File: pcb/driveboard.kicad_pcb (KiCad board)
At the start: 2 copper layers, 147.3 x 94 mm, 53 parts, among them IC1 7411, IC2 7410, P1 AC IN, P2 AC out, P3 5V in, P6 AQV2526, x1 RJ45, x2 RJ45, y1 RJ45, y2 RJ45

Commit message: Use Protel filename extensions for the sake of dirtypcbs.com.
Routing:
- net Net-(R12-Pad2): track 20.9 -> 31.7 mm
- net Net-(Arduino2-Pad2): track 46.4 -> 35.6 mm

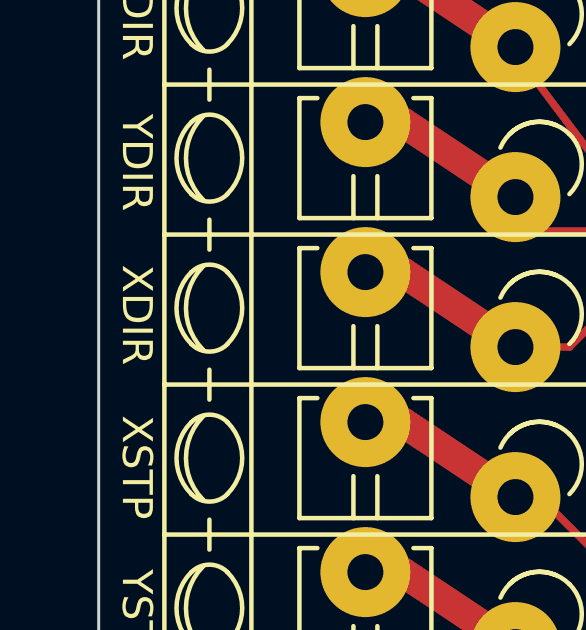
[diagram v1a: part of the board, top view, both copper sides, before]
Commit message: Fix wrong label.
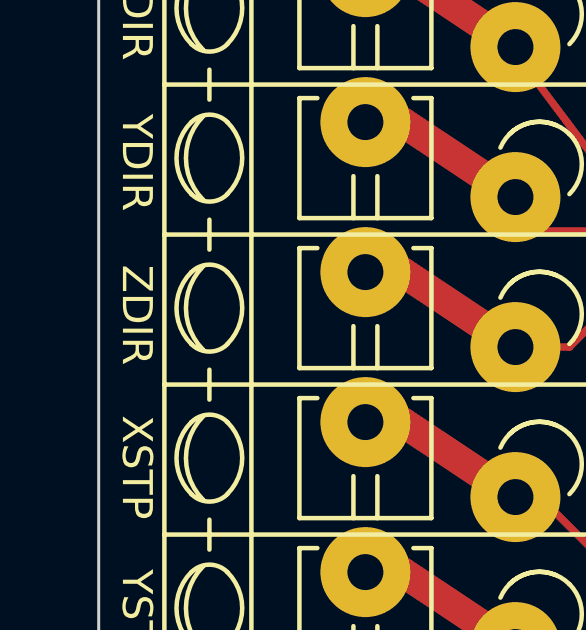
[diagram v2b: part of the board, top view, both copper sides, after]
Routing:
- net Net-(Arduino2-Pad2): track 35.6 -> 44.9 mm
- net Net-(R12-Pad2): track 31.7 -> 22.4 mm
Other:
- board text added: "ZDIR"
